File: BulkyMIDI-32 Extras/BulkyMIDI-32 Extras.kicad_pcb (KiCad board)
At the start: 2 copper layers, 100 x 100 mm, 68 parts, among them J1 DC IN, J10 MIDI2, J11 MIDI3, J12 SERIAL, J13 ICSP, J14 BIN/ASCII, J15 BAUD RATE, J16 Stacked RS232 Module, J2 MIDI OUT, J3 MIDI IN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

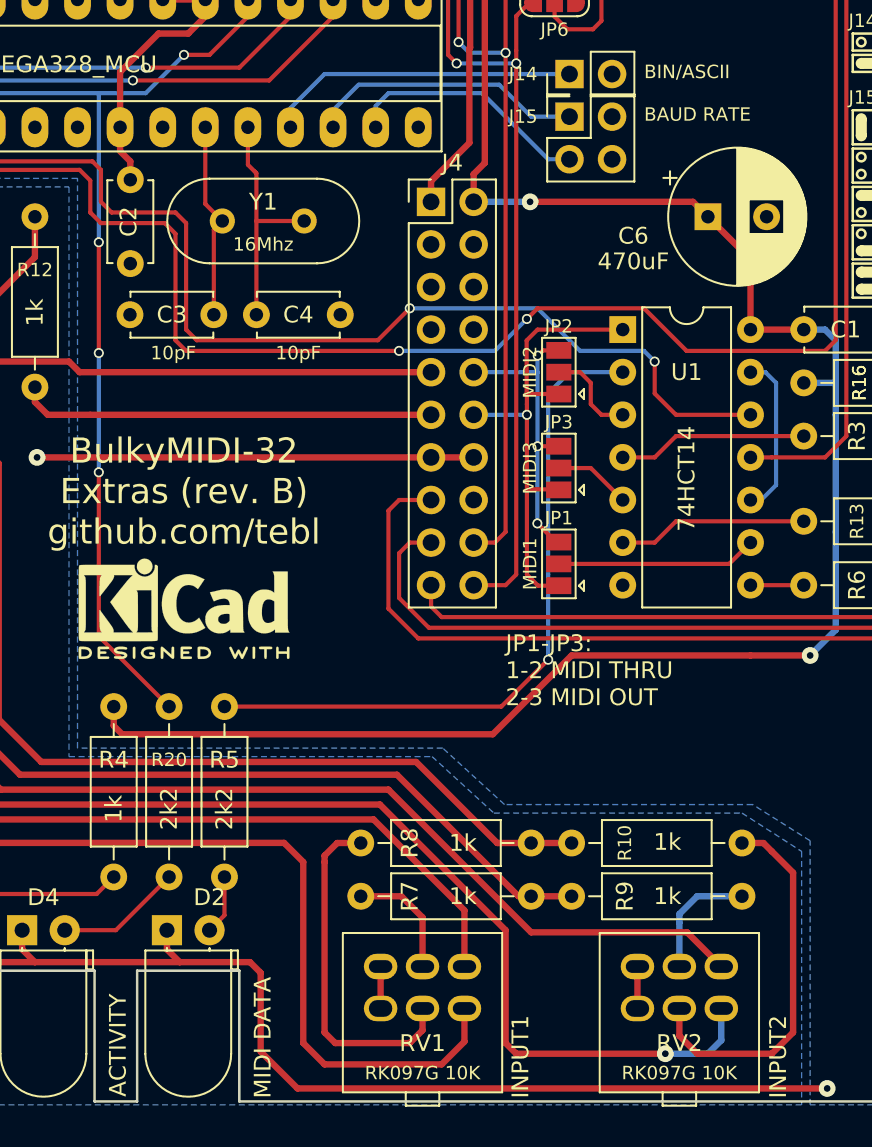
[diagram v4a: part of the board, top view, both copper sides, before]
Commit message: Better LED naming
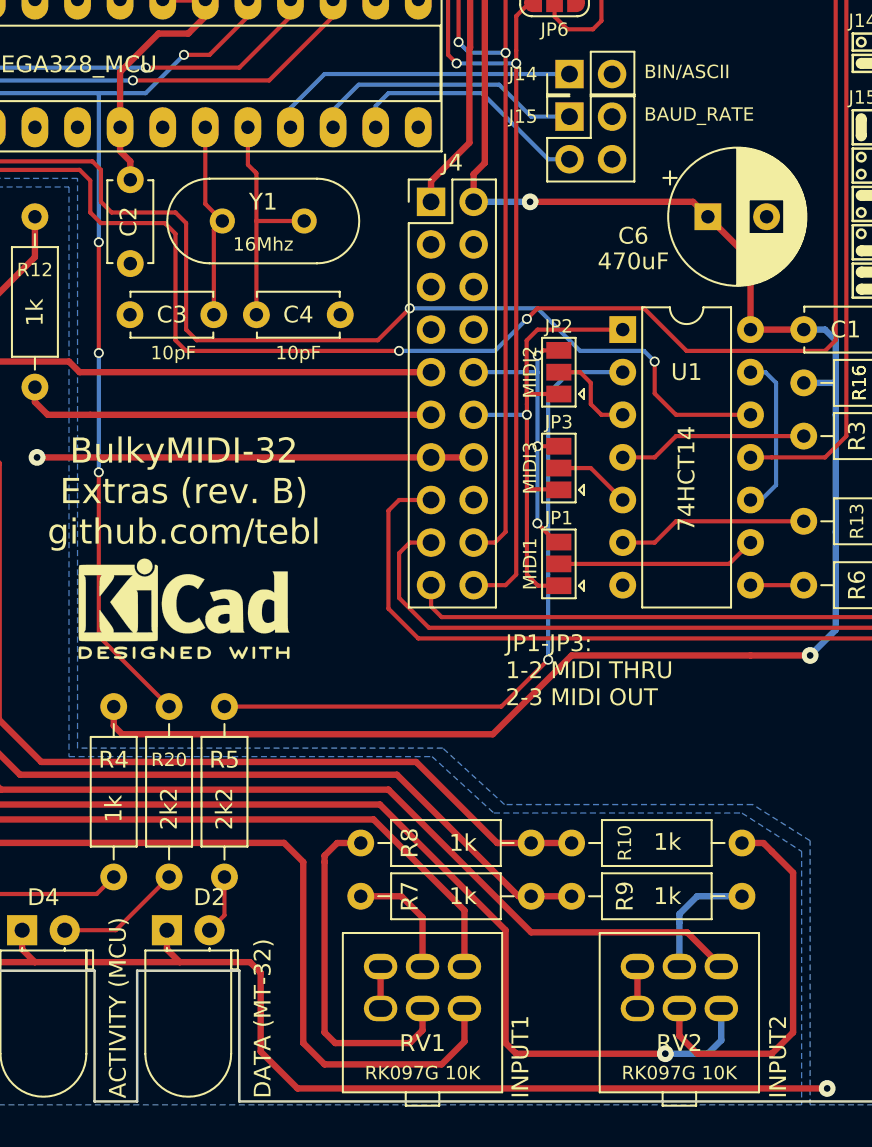
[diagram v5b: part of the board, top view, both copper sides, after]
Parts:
- D2: value MIDI DATA -> DATA (MT-32)
- D4: value ACTIVITY -> ACTIVITY (MCU)
- J15: value BAUD RATE -> BAUD_RATE

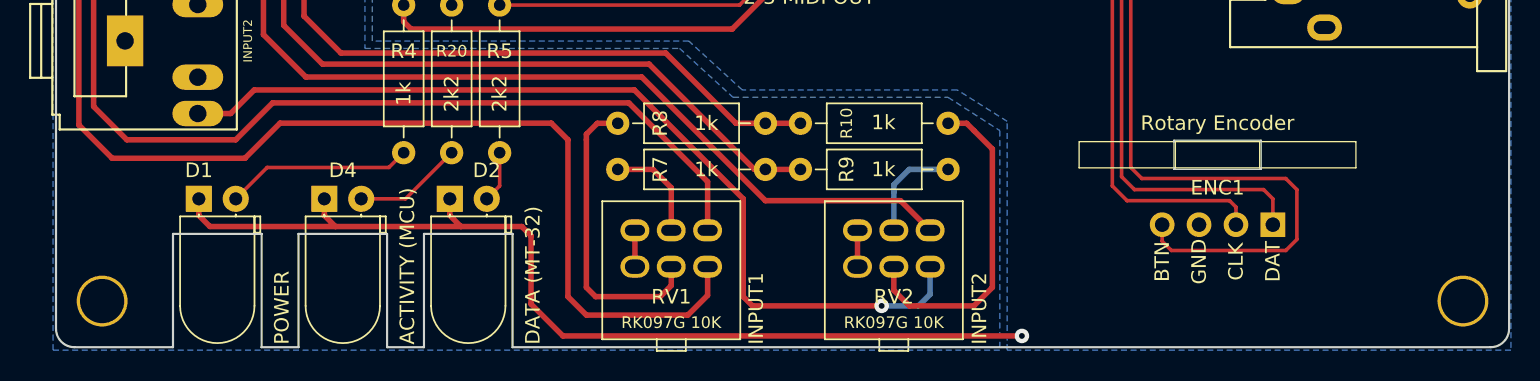
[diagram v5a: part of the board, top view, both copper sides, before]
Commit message: Moved input2 to make space for cap
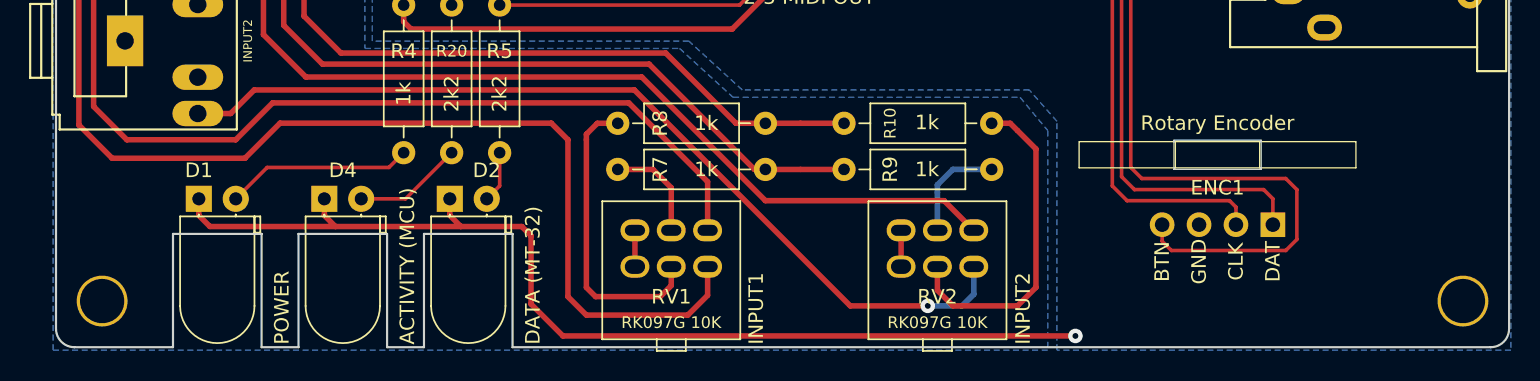
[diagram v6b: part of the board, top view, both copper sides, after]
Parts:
- moved R10 3.00 mm to (134.6, 139.2)
- moved R9 3.00 mm to (124.4, 142.4)
- moved RV2 3.00 mm to (130.8, 146.6)
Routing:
- net GND: track 69.0 -> 72.7 mm
- net /RIGHT: track 84.2 -> 87.2 mm
- net /LEFT: track 75.3 -> 78.3 mm
- net /I2_R: track 59.5 -> 62.5 mm
- net /I2_L: track 63.4 -> 62.6 mm

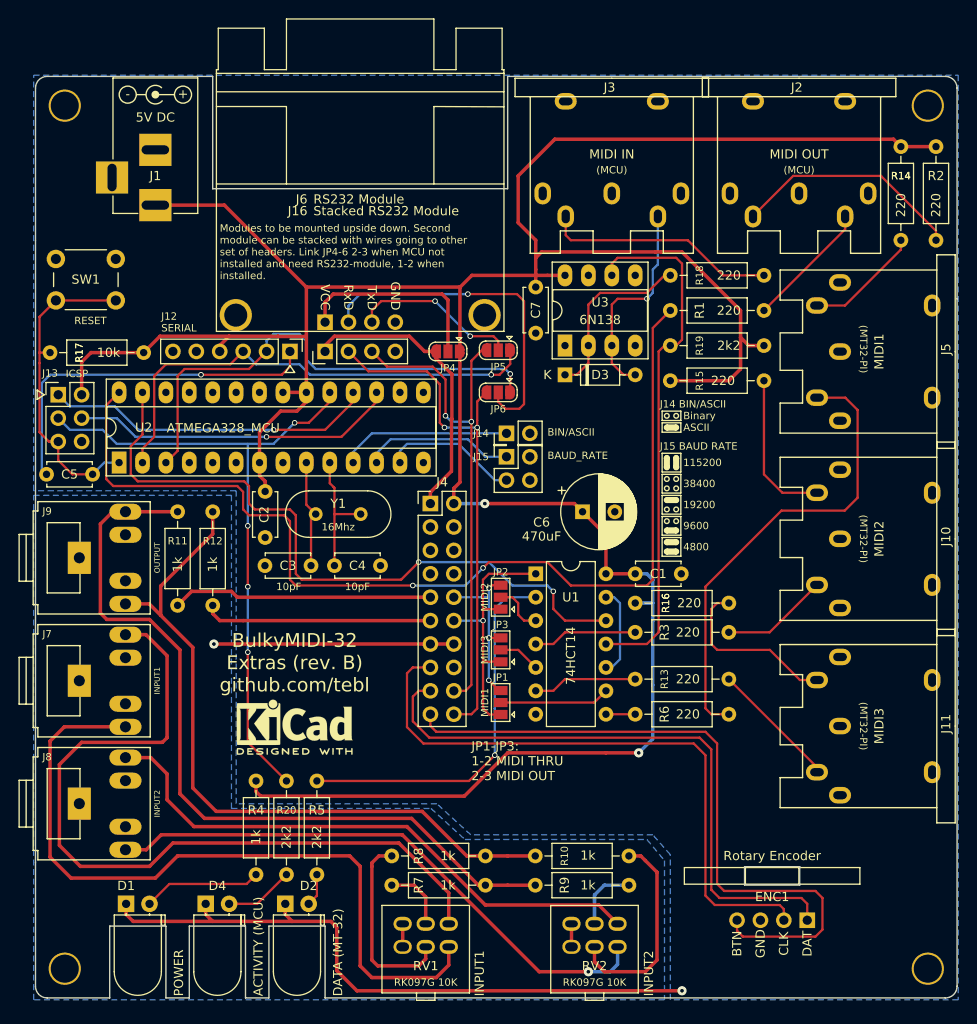
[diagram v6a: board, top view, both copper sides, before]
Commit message: Made DATA LED a bit nicer, moved rotary encoder slightly
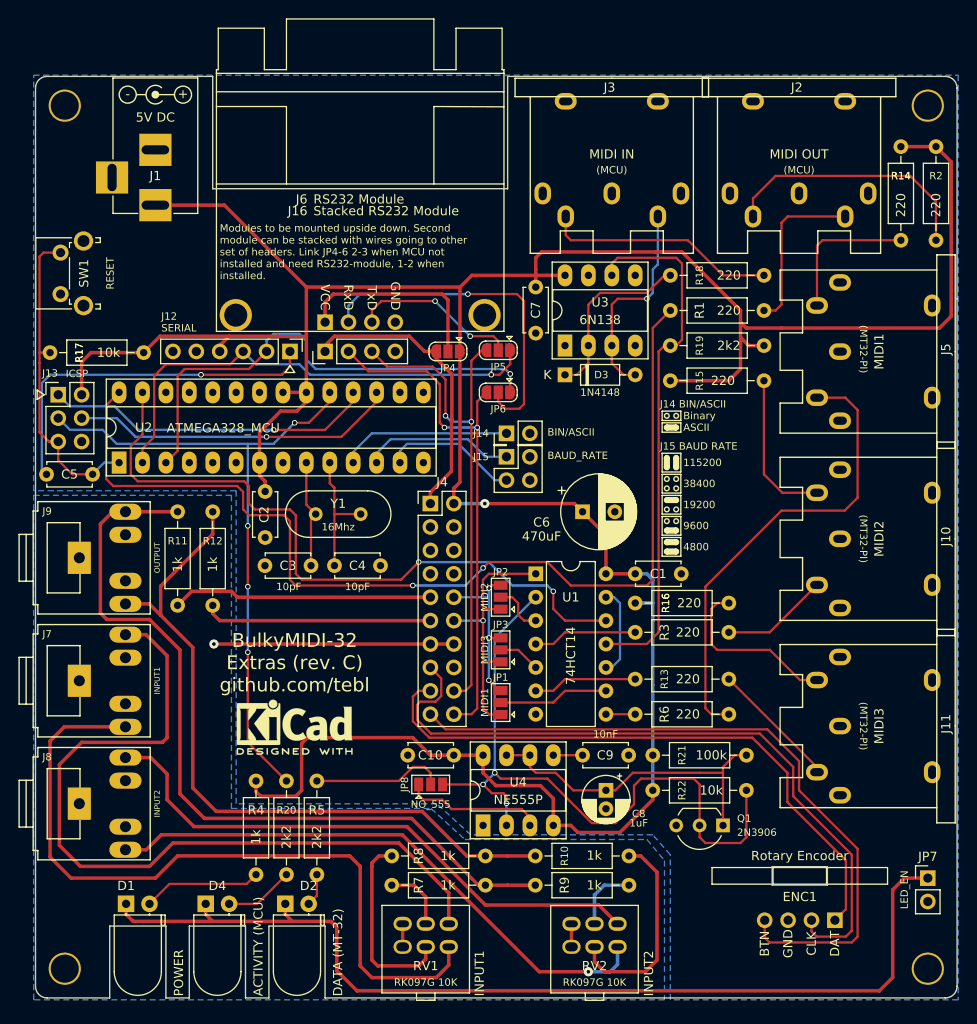
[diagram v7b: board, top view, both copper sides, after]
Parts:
- removed G***: LOGO, artwork:BulkyMIDI-32
- added C10: 100nF, Capacitor_THT:C_Disc_D4.7mm_W2.5mm_P5.00mm, F.Cu at (115.6, 128.3)
- added C8: 1uF, Capacitor_THT:CP_Radial_D5.0mm_P2.00mm, F.Cu at (132.1, 132.1)
- added C9: 10nF, Capacitor_THT:C_Disc_D4.7mm_W2.5mm_P5.00mm, F.Cu at (134.5, 128.3)
- added JP7: LED_EN, Connector_PinHeader_2.54mm:PinHeader_1x02_P2.54mm_Vertical, F.Cu at (167.0, 141.6)
- added JP8: NO_555, Jumper:SolderJumper-3_P1.3mm_Open_Pad1.0x1.5mm, F.Cu at (113.1, 131.4)
- added Q1: 2N3906, Package_TO_SOT_THT:TO-92_Inline_Wide, F.Cu at (144.8, 135.9)
- added R21: 100k, Resistor_THT:R_Axial_DIN0207_L6.3mm_D2.5mm_P10.16mm_Horizontal, F.Cu at (147.3, 128.3)
- added R22: 10k, Resistor_THT:R_Axial_DIN0207_L6.3mm_D2.5mm_P10.16mm_Horizontal, F.Cu at (147.3, 132.1)
- added U4: NE555P, Package_DIP:DIP-8_W7.62mm_Socket_LongPads, F.Cu at (118.7, 135.9)
- SW1: footprint Button_Switch_THT:SW_PUSH_6mm -> Button_Switch_THT:SW_Tactile_SPST_Angled_PTS645Vx39-2LFS
- moved SW1 3.84 mm to (72.9, 78.2), turned to 90 degrees
- moved ENC1 3.00 mm to (153.1, 146.2)
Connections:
- D1 pad 1: GND -> Net-(D1-Pad1)
- D2 pad 1: GND -> Net-(D1-Pad1)
- D4 pad 1: GND -> Net-(D1-Pad1)
- R5 pad 2: Net-(R5-Pad2) -> Net-(JP8-Pad2)
- U1 pad 2: Net-(R5-Pad2) -> LED_DATA
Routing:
- net Net-(D1-Pad1): track 0.00 -> 110.0 mm
- net LED_DATA: track 0.00 -> 77.7 mm, vias 0 -> 3
- net GND: track 72.7 -> 0.00 mm, vias 1 -> 0
- net Net-(R5-Pad2): track 41.3 -> 0.00 mm, vias 1 -> 0
- net Net-(C8-Pad1): track 0.00 -> 36.0 mm
- net Net-(JP8-Pad1): track 0.00 -> 15.1 mm
- net Net-(JP8-Pad2): track 0.00 -> 14.5 mm
- net SW_DOWN: track 67.9 -> 77.7 mm
- net +5V: track 328.1 -> 335.8 mm, vias 2 -> 1
- net Net-(J2-Pad5): track 14.5 -> 18.9 mm
- net Net-(J5-Pad4): track 12.6 -> 15.8 mm
- net Net-(C9-Pad2): track 0.00 -> 3.17 mm
- net Net-(J2-Pad4): track 25.2 -> 28.2 mm
- net SW_ENC: track 74.9 -> 76.2 mm
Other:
- outline, holes or cut-outs redrawn
- board text added: "BulkyMIDI-32 Extras (rev. C) github.com/tebl"
- board text added: "MCU RESET"
- board text removed: "BulkyMIDI-32 Extras (rev. B) github.com/tebl"
